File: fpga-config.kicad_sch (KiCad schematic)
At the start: 32 parts, among them J1 878321412, Q1 BSS138W-7-F, Q2 BSS138W-7-F, SW1 CVS-03B, U1 XC7K410T-2FFG900I, U2 TPD4E05U06QDQARQ1, U3 MAX1617AMEE+T

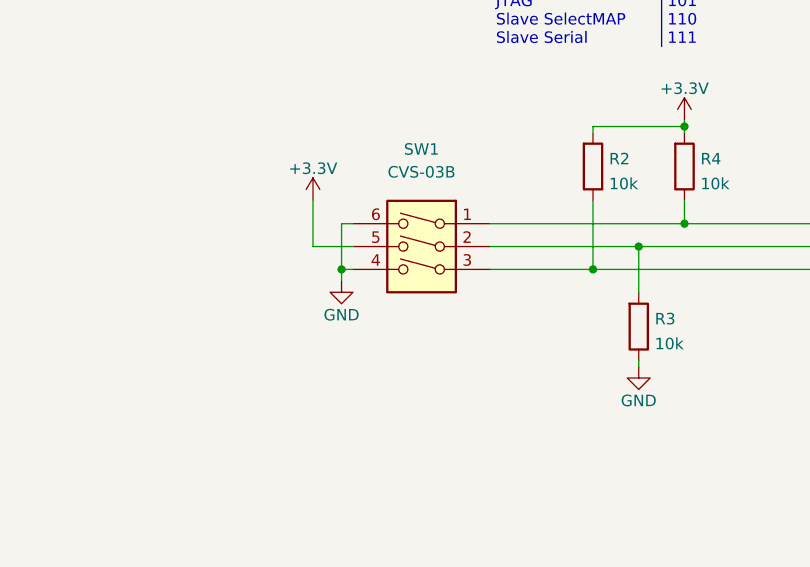
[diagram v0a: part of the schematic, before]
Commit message: Updated all symbols causing warnings with no signal connected to pad, added thermal vias on level shifters' thermal pad with small tweaks on signal routing near this area
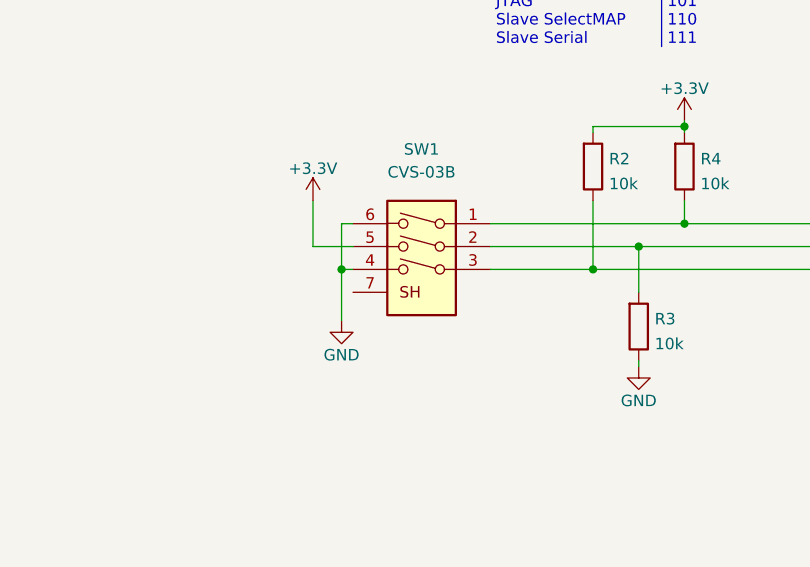
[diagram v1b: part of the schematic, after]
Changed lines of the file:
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@@
     (stroke (width 0) (type default) (color 0 0 0 0))
   )
-  (wire (pts (xy 81.915 135.89) (xy 81.915 137.16))
+  (wire (pts (xy 81.915 135.89) (xy 81.915 141.605))
     (stroke (width 0) (type default) (color 0 0 0 0))
   )
@@
     (pin "5")
     (pin "6")
+    (pin "7")
   )
   (symbol (lib_id "K410T-devboard:R_10k_0402") (at 312.42 169.545 90) (unit 1)
@@
     (pin "1")
   )
-  (symbol (lib_id "K410T-devboard:GND") (at 81.915 137.16 0) (mirror y) (unit 1)
+  (symbol (lib_id "K410T-devboard:GND") (at 81.915 141.605 0) (mirror y) (unit 1)
     (in_bom yes) (on_board yes)
-    (property "Reference" "#PWR045" (id 0) (at 81.915 143.51 0)
+    (property "Reference" "#PWR045" (id 0) (at 81.915 147.955 0)
       (effects (font (size 1.27 1.27)) hide)
     )
-    (property "Value" "GND" (id 1) (at 81.915 140.97 0))
-    (property "Footprint" "" (id 2) (at 81.915 137.16 0)
+    (property "Value" "GND" (id 1) (at 81.915 145.415 0))
+    (property "Footprint" "" (id 2) (at 81.915 141.605 0)
       (effects (font (size 1.27 1.27)) hide)
     )
-    (property "Datasheet" "" (id 3) (at 81.915 137.16 0)
+    (property "Datasheet" "" (id 3) (at 81.915 141.605 0)
       (effects (font (size 1.27 1.27)) hide)
     )
